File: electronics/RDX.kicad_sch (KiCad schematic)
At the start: 59 parts, among them J1 Conn_WallSocket_Earth, M1 Fan_3pin, SW1 SW_DPST

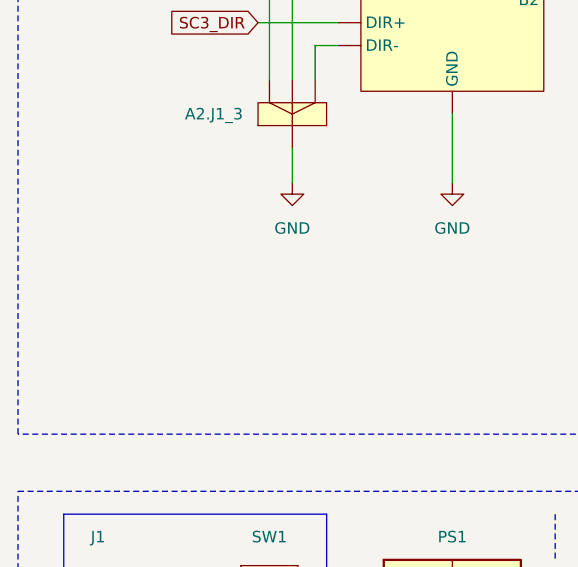
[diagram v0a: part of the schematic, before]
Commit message: further printing and building progress with documentation updates
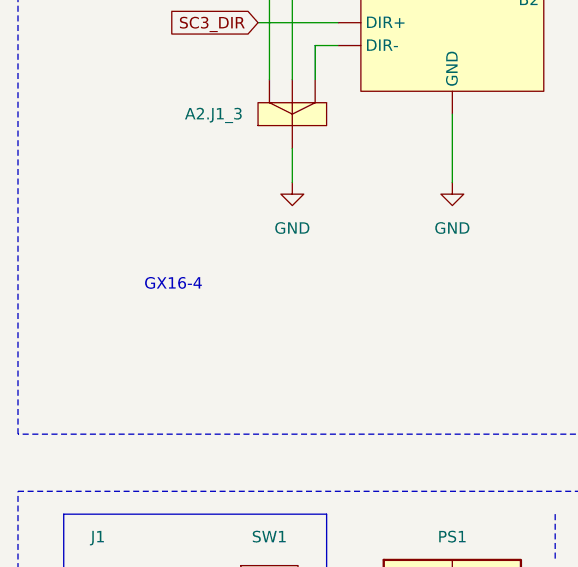
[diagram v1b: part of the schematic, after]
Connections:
- new net: A2.J1_2., A2.U1_2. (B2) (x3)
- new net: A2.J1_4., A2.U1_4. (B2) (x3)
- new net: A3.J3., A5.U1_1. (B2)
- new net: A3.J2., A5.U1_1. (B2)
- new net: A2.J1_1., A2.U1_1. (B2) (x3)
- new net: A2.J1_3., A2.U1_3. (B2) (x3)
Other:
- note added: "GX16-4"
